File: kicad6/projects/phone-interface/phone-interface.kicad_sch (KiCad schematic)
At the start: 17 parts, among them J1 Screw_Terminal_01x02, J2 Screw_Terminal_01x02, J3 Screw_Terminal_01x04, Q1 IRLU8256PbF, Q2 IRLU8256PbF, T1 2x 9V 0.5VA, U1 R-78E5.0-0.5

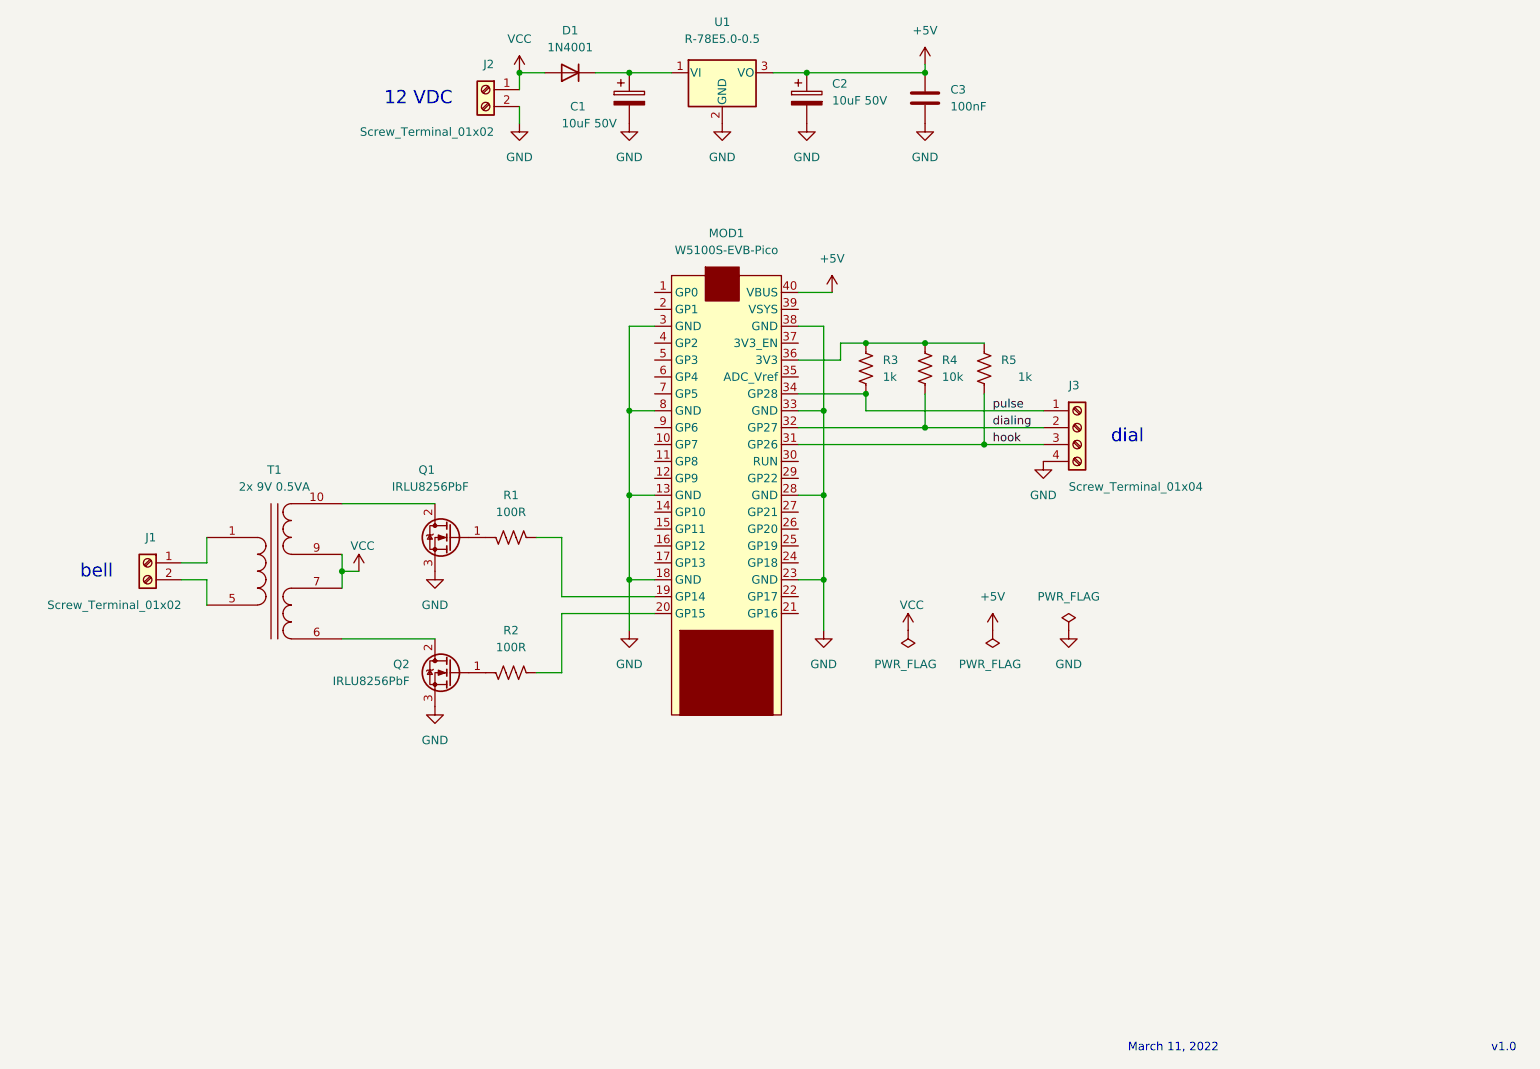
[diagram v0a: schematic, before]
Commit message: Add files via upload
- Corrected connections of bell HV converter
- Added LED to pin 6.
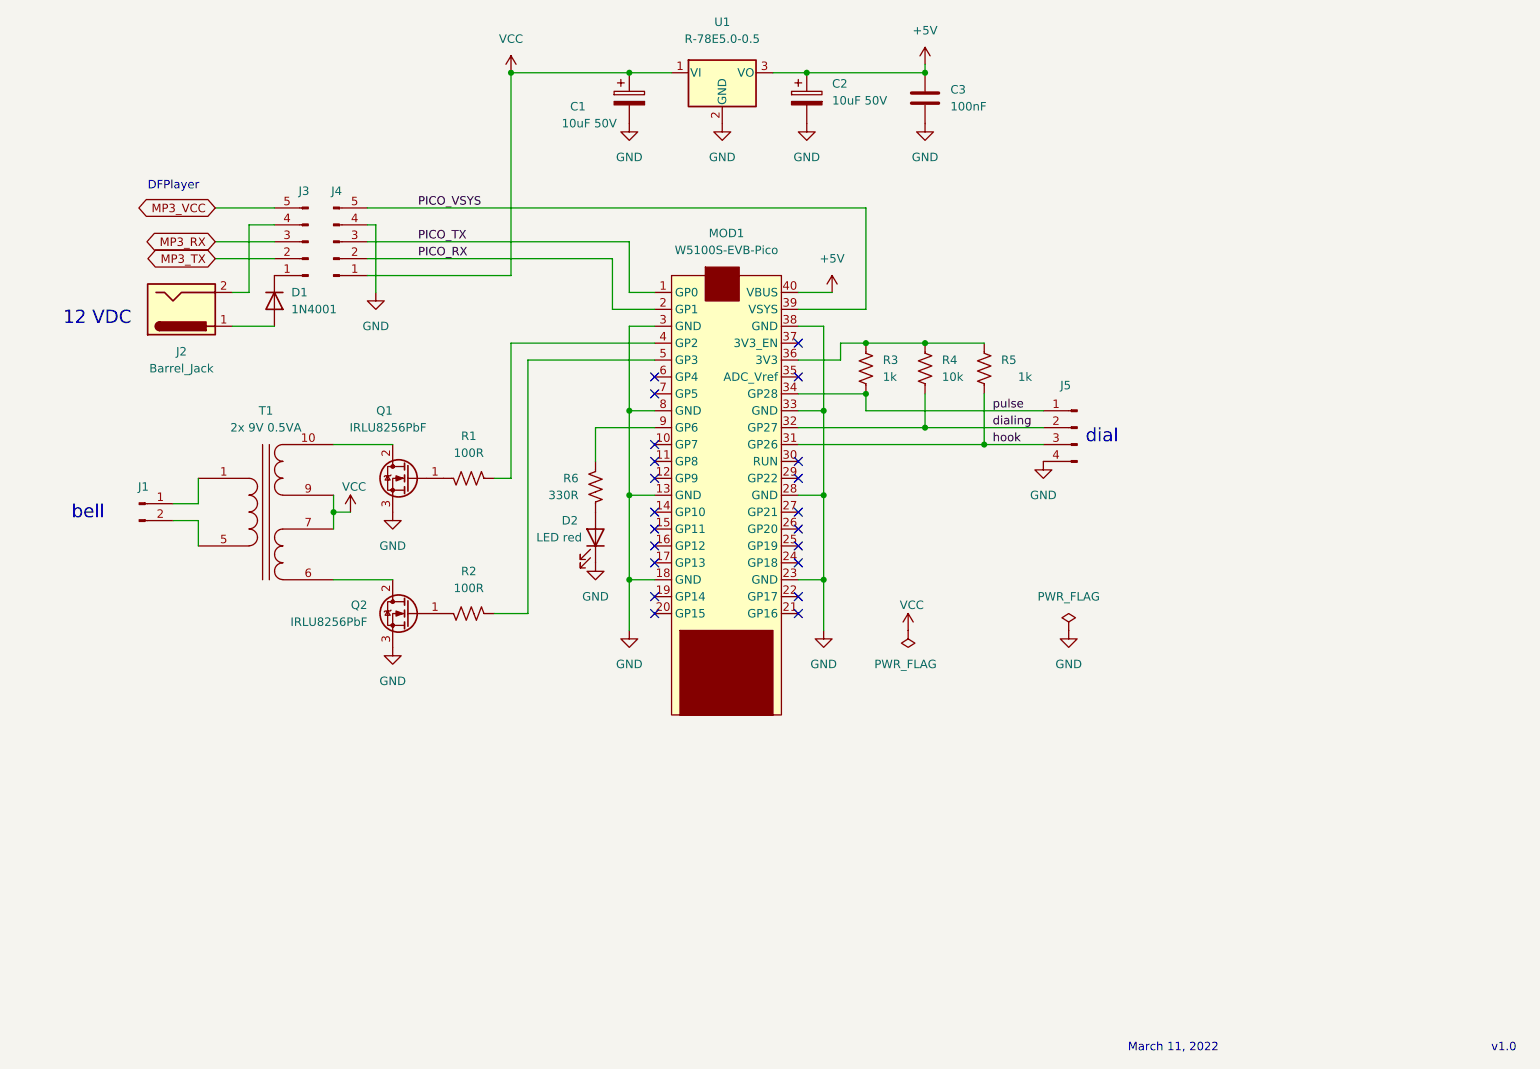
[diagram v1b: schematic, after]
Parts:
- removed J1, J2: Screw_Terminal_01x02, TerminalBlock_MetzConnect:TerminalBlock_MetzConnect_Type101_RT01602HBWC_1x02_P5.08mm_Horizontal, symbol Connector:Screw_Terminal_01x02
- removed J3: Screw_Terminal_01x04, TerminalBlock_MetzConnect:TerminalBlock_MetzConnect_Type101_RT01604HBWC_1x04_P5.08mm_Horizontal, symbol Connector:Screw_Terminal_01x04
- added D2: LED red, symbol Device:LED
- added J1: Conn_01x02_Male, symbol Connector:Conn_01x02_Male
- added J2: Barrel_Jack, symbol Connector:Barrel_Jack
- added J3, J4: Conn_01x05_Male, symbol Connector:Conn_01x05_Male
- added J5: Conn_01x04_Male, symbol Connector:Conn_01x04_Male
- added R6: 330R, Resistor_SMD:R_0805_2012Metric_Pad1.20x1.40mm_HandSolder, symbol Device:R_US
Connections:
- net GND: now also D2.1 (K), J4.4 (Pin_4), J5.4 (Pin_4)
- net VCC: now also C1.1, U1.1 (VI), J4.1 (Pin_1); no longer D1.2 (A)
- net dialing: now also J5.2 (Pin_2)
- net hook: now also J5.3 (Pin_3)
- net pulse: now also J5.1 (Pin_1)
- net at T1.1 (AA): now also J1.1 (Pin_1)
- net at T1.5 (AB): now also J1.2 (Pin_2)
- net PICO_TX: now reaches MOD1.1 (GP0)
- net PICO_TX: now also J4.3 (Pin_3)
- net at MOD1.19 (GP14): no longer R1.1
- net PICO_RX: now reaches MOD1.2 (GP1)
- net PICO_RX: now also J4.2 (Pin_2)
- net at MOD1.20 (GP15): no longer R2.1
- net PICO_VSYS: now reaches MOD1.39 (VSYS)
- net PICO_VSYS: now also J4.5 (Pin_5)
- net at MOD1.4 (GP2): now also R1.1
- net at MOD1.5 (GP3): now also R2.1
- net at MOD1.9 (GP6): now also R6.2
- new net: D1.1 (K), J3.1 (Pin_1)
- new net: D1.2 (A), J2.1
- new net: J2.2, J3.4 (Pin_4)
- new net: D2.2 (A), R6.1
- new net MP3_RX: J3.3 (Pin_3)
- new net MP3_TX: J3.2 (Pin_2)
- new net MP3_VCC: J3.5 (Pin_5)
- no-connect marks 0 -> 21
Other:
- note added: "DFPlayer"
- moved on the sheet: D1, Q1, Q2, R1, R2, T1
